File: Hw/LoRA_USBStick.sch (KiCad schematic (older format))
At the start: 16 parts, among them J10 USB_B, J4 SWD, SW1 RST, U1 ATSAMD21E, U2 RFM95W-868S2, U3 AP2112K-3.3

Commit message: add usb c and R
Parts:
- removed J10: USB_B, Connectors:C46394, symbol LoRA_USBStick-rescue:USB_B
- added P1: USB_C_Plug_USB2.0, symbol Connector:USB_C_Plug_USB2.0
- added R1, R2: 5K1, symbol Device:R
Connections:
- wire segments 57 -> 66
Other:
- moved on the sheet: J4
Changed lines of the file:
@@
 EESchema Schematic File Version 4
+LIBS:LoRA_USBStick-cache
 EELAYER 30 0
 EELAYER END
@@
 	1    0    0    -1
 $EndComp
-$Comp
-L LoRA_USBStick-rescue:Conn_01x04 J4
-U 1 1 5B0502EC
-P 6300 4805
-F 0 "J4" H 6300 5005 50  0000 C CNN
-F 1 "SWD" H 6300 4505 50  0000 C CNN
-F 2 "Pin_Headers:Pin_Header_Straight_1x04_Pitch2.54mm" H 6300 4805 50  0001 C CNN
-F 3 "" H 6300 4805 50  0001 C CNN
-	1    6300 4805
-	1    0    0    -1
-$EndComp
-$Comp
-L power:+3.3V #PWR012
-U 1 1 5B050850
-P 5955 4625
-F 0 "#PWR012" H 5955 4475 50  0001 C CNN
-F 1 "+3.3V" H 5955 4765 50  0000 C CNN
-F 2 "" H 5955 4625 50  0001 C CNN
-F 3 "" H 5955 4625 50  0001 C CNN
-	1    5955 4625
-	1    0    0    -1
-$EndComp
-Text Label 5955 4905 2    60   ~ 0
-SWCLK
-Text Label 5955 4805 2    60   ~ 0
-SWDIO
 Text Label 6965 4065 0    60   ~ 0
 SWDIO
@@
 Wire Wire Line
 	4820 1535 4895 1535
-Wire Wire Line
-	6100 4905 5955 4905
-Wire Wire Line
-	5955 4805 6100 4805
-Wire Wire Line
-	6100 4705 5955 4705
-Wire Wire Line
-	5955 4705 5955 4625
-Wire Wire Line
-	5965 5080 5965 5005
-Wire Wire Line
-	5965 5005 6100 5005
 Wire Wire Line
 	7680 725  7680 825
@@
 Wire Notes Line
 	11220 4565 11220 4560
-$Comp
-L power:GND #PWR014
-U 1 1 5B08A6AC
-P 5965 5080
-F 0 "#PWR014" H 5965 4830 50  0001 C CNN
-F 1 "GND" H 5965 4930 50  0000 C CNN
-F 2 "" H 5965 5080 50  0001 C CNN
-F 3 "" H 5965 5080 50  0001 C CNN
-	1    5965 5080
-	1    0    0    -1
-$EndComp
 Text Label 6965 2665 0    60   ~ 0
 RFM_RST
@@
 L power:GND #PWR015
 U 1 1 5B0C9EAC
-P 4805 5395
-F 0 "#PWR015" H 4805 5145 50  0001 C CNN
-F 1 "GND" H 4805 5245 50  0000 C CNN
-F 2 "" H 4805 5395 50  0001 C CNN
-F 3 "" H 4805 5395 50  0001 C CNN
-	1    4805 5395
-	1    0    0    -1
-$EndComp
-Wire Wire Line
-	4805 5395 4805 5350
-Wire Wire Line
-	4905 5290 4905 5350
-Wire Wire Line
-	4905 5350 4805 5350
-Connection ~ 4805 5350
-Text Label 5205 4890 0    60   ~ 0
+P 4780 6236
+F 0 "#PWR015" H 4780 5986 50  0001 C CNN
+F 1 "GND" H 4780 6086 50  0000 C CNN
+F 2 "" H 4780 6236 50  0001 C CNN
+F 3 "" H 4780 6236 50  0001 C CNN
+	1    4780 6236
+	1    0    0    -1
+$EndComp
+Text Label 5528 5292 0    60   ~ 0
 D+
-Text Label 5205 4990 0    60   ~ 0
+Text Label 5528 5092 0    60   ~ 0
 D-
 Text Label 6965 3665 0    60   ~ 0
@@
 Text Label 6965 3565 0    60   ~ 0
 D-
-$Comp
-L power:VBUS #PWR016
-U 1 1 5B0CB923
-P 5285 4630
-F 0 "#PWR016" H 5285 4480 50  0001 C CNN
-F 1 "VBUS" H 5285 4780 50  0000 C CNN
-F 2 "" H 5285 4630 50  0001 C CNN
-F 3 "" H 5285 4630 50  0001 C CNN
-	1    5285 4630
-	1    0    0    -1
-$EndComp
-Wire Wire Line
-	5285 4630 5285 4690
-Wire Wire Line
-	5285 4690 5205 4690
 Text Notes 1165 935  0    60   ~ 0
 USB voltage regulator\n
@@
 NoConn ~ 6965 1865
 NoConn ~ 6965 1165
-$Comp
-L LoRA_USBStick-rescue:USB_B J10
-U 1 1 5B11F4BB
-P 4905 4890
-F 0 "J10" H 4705 5340 50  0000 L CNN
-F 1 "USB_B" H 4705 5240 50  0000 L CNN
-F 2 "Connectors:C46394" H 5055 4840 50  0001 C CNN
-F 3 "" H 5055 4840 50  0001 C CNN
-	1    4905 4890
-	1    0    0    -1
-$EndComp
 Wire Wire Line
 	10750 1950 10750 2050
@@
 	4650 1255 4650 1385
 Wire Wire Line
-	4805 5350 4805 5290
-Wire Wire Line
 	2355 1330 2960 1330
 Wire Wire Line
 	1395 1330 1315 1330
-Wire Notes Line
-	8270 475  8270 6535
 Wire Notes Line
 	2290 2365 2290 6540
@@
 	1565 1430 1565 1330
 Connection ~ 1565 1330
+$Comp
+L Connector:USB_C_Plug_USB2.0 P1
+U 1 1 5F54D8FB
+P 4928 5192
+F 0 "P1" H 5035 6059 50  0000 C CNN
+F 1 "USB_C_Plug_USB2.0" H 5035 5968 50  0000 C CNN
+F 2 "" H 5078 5192 50  0001 C CNN
+F 3 "https://www.usb.org/sites/default/files/documents/usb_type-c.zip" H 5078 5192 50  0001 C CNN
+	1    4928 5192
+	1    0    0    -1
+$EndComp
+$Comp
+L power:VBUS #PWR016
+U 1 1 5B0CB923
+P 5607 4533
+F 0 "#PWR016" H 5607 4383 50  0001 C CNN
+F 1 "VBUS" H 5607 4683 50  0000 C CNN
+F 2 "" H 5607 4533 50  0001 C CNN
+F 3 "" H 5607 4533 50  0001 C CNN
+	1    5607 4533
+	1    0    0    -1
+$EndComp
+Wire Wire Line
+	5607 4533 5607 4592
+Wire Wire Line
+	5607 4592 5528 4592
+Wire Wire Line
+	4628 6092 4628 6161
+Wire Wire Line
+	4628 6161 4780 6161
+Wire Wire Line
+	4928 6092 4928 6161
+Wire Wire Line
+	4780 6236 4780 6161
+Connection ~ 4780 6161
+Wire Wire Line
+	4780 6161 4928 6161
+$Comp
+L Device:R R2
+U 1 1 5F5760B6
+P 5834 4892
+F 0 "R2" V 5912 4893 50  0000 C CNN
+F 1 "5K1" V 5990 4899 50  0000 C CNN
+F 2 "" V 5764 4892 50  0001 C CNN
+F 3 "~" H 5834 4892 50  0001 C CNN
+	1    5834 4892
+	0    1    1    0
+$EndComp
+Wire Wire Line
+	5528 4792 5684 4792
+Wire Wire Line
+	5684 4892 5528 4892
+$Comp
+L power:GND #PWR011
+U 1 1 5F57D4B7
+P 6111 4904
+F 0 "#PWR011" H 6111 4654 50  0001 C CNN
+F 1 "GND" H 6111 4754 50  0000 C CNN
+F 2 "" H 6111 4904 50  0001 C CNN
+F 3 "" H 6111 4904 50  0001 C CNN
+	1    6111 4904
+	1    0    0    -1
+$EndComp
+Wire Wire Line
+	5984 4892 6032 4892
+Wire Wire Line
+	6032 4792 5984 4792
+Wire Wire Line
+	6032 4892 6032 4837
+Wire Wire Line
+	6111 4904 6111 4837
+Wire Wire Line
+	6111 4837 6032 4837
+Connection ~ 6032 4837
+Wire Wire Line
+	6032 4837 6032 4792
+$Comp
+L LoRA_USBStick-rescue:Conn_01x04 J4
+U 1 1 5B0502EC
+P 7145 5321
+F 0 "J4" H 7145 5521 50  0000 C CNN
+F 1 "SWD" H 7145 5021 50  0000 C CNN
+F 2 "Pin_Headers:Pin_Header_Straight_1x04_Pitch2.54mm" H 7145 5321 50  0001 C CNN
+F 3 "" H 7145 5321 50  0001 C CNN
+	1    7145 5321
+	1    0    0    -1
+$EndComp
+$Comp
+L power:+3.3V #PWR012
+U 1 1 5B050850
+P 6800 5141
+F 0 "#PWR012" H 6800 4991 50  0001 C CNN
+F 1 "+3.3V" H 6800 5281 50  0000 C CNN
+F 2 "" H 6800 5141 50  0001 C CNN
+F 3 "" H 6800 5141 50  0001 C CNN
+	1    6800 5141
+	1    0    0    -1
+$EndComp
+Text Label 6800 5421 2    60   ~ 0
+SWCLK
+Text Label 6800 5321 2    60   ~ 0
+SWDIO
+Wire Wire Line
+	6945 5421 6800 5421
+Wire Wire Line
+	6800 5321 6945 5321
+Wire Wire Line
+	6945 5221 6800 5221
+Wire Wire Line
+	6800 5221 6800 5141
+Wire Wire Line
+	6810 5596 6810 5521
+Wire Wire Line
+	6810 5521 6945 5521
+$Comp
+L power:GND #PWR014
+U 1 1 5B08A6AC
+P 6810 5596
+F 0 "#PWR014" H 6810 5346 50  0001 C CNN
+F 1 "GND" H 6810 5446 50  0000 C CNN
+F 2 "" H 6810 5596 50  0001 C CNN
+F 3 "" H 6810 5596 50  0001 C CNN
+	1    6810 5596
+	1    0    0    -1
+$EndComp
+Wire Notes Line
+	8270 475  8270 6535
+$Comp
+L Device:R R1
+U 1 1 5F575919
+P 5834 4792
+F 0 "R1" V 5627 4792 50  0000 C CNN
+F 1 "5K1" V 5718 4792 50  0000 C CNN
+F 2 "" V 5764 4792 50  0001 C CNN
+F 3 "~" H 5834 4792 50  0001 C CNN
+	1    5834 4792
+	0    1    1    0
+$EndComp
 $EndSCHEMATC

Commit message: Change_usb-C
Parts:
- P1: footprint (none) -> Connectors:C393939
- R1, R2: footprint (none) -> Resistor_SMD:R_0603_1608Metric_Pad1.05x0.95mm_HandSolder
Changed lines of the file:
@@
 F 0 "P1" H 5035 6059 50  0000 C CNN
 F 1 "USB_C_Plug_USB2.0" H 5035 5968 50  0000 C CNN
-F 2 "" H 5078 5192 50  0001 C CNN
+F 2 "Connectors:C393939" H 5078 5192 50  0001 C CNN
 F 3 "https://www.usb.org/sites/default/files/documents/usb_type-c.zip" H 5078 5192 50  0001 C CNN
 	1    4928 5192
@@
 F 0 "R2" V 5912 4893 50  0000 C CNN
 F 1 "5K1" V 5990 4899 50  0000 C CNN
-F 2 "" V 5764 4892 50  0001 C CNN
+F 2 "Resistor_SMD:R_0603_1608Metric_Pad1.05x0.95mm_HandSolder" V 5764 4892 50  0001 C CNN
 F 3 "~" H 5834 4892 50  0001 C CNN
 	1    5834 4892
@@
 F 0 "R1" V 5627 4792 50  0000 C CNN
 F 1 "5K1" V 5718 4792 50  0000 C CNN
-F 2 "" V 5764 4792 50  0001 C CNN
+F 2 "Resistor_SMD:R_0603_1608Metric_Pad1.05x0.95mm_HandSolder" V 5764 4792 50  0001 C CNN
 F 3 "~" H 5834 4792 50  0001 C CNN
 	1    5834 4792

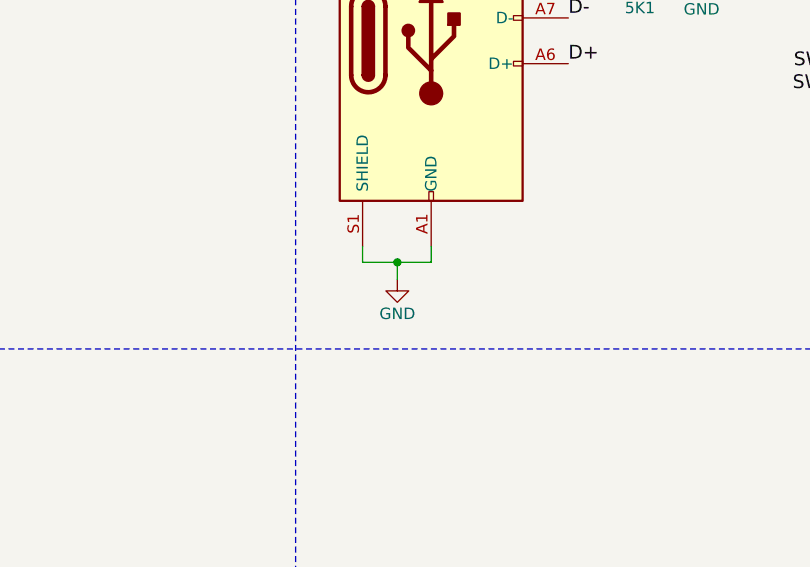
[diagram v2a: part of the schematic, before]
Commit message: Change_in_connector
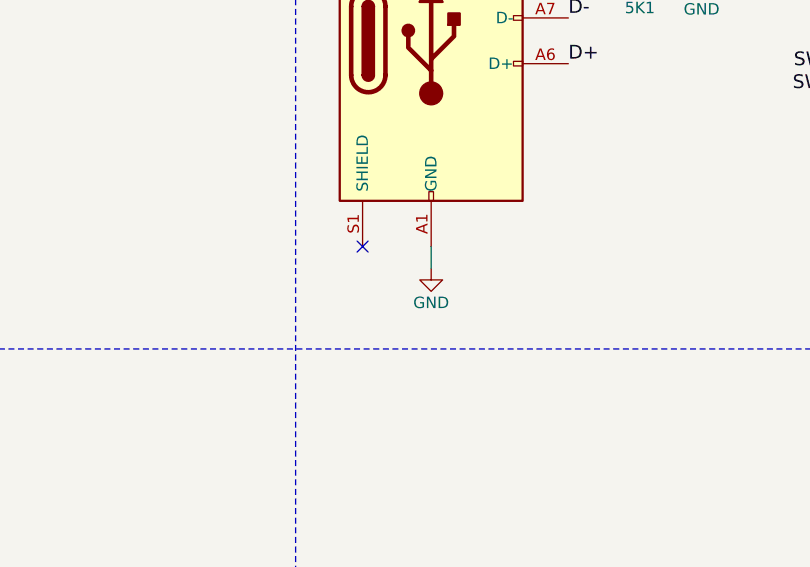
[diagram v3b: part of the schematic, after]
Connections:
- net GND: no longer P1.S1 (SHIELD)
- no-connect marks 14 -> 15
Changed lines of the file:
@@
 EESchema Schematic File Version 4
-LIBS:LoRA_USBStick-cache
 EELAYER 30 0
 EELAYER END
@@
 Text Label 6965 2665 0    60   ~ 0
 RFM_RST
-$Comp
-L power:GND #PWR015
-U 1 1 5B0C9EAC
-P 4780 6236
-F 0 "#PWR015" H 4780 5986 50  0001 C CNN
-F 1 "GND" H 4780 6086 50  0000 C CNN
-F 2 "" H 4780 6236 50  0001 C CNN
-F 3 "" H 4780 6236 50  0001 C CNN
-	1    4780 6236
-	1    0    0    -1
-$EndComp
 Text Label 5528 5292 0    60   ~ 0
 D+
@@
 Wire Wire Line
 	5607 4592 5528 4592
-Wire Wire Line
-	4628 6092 4628 6161
-Wire Wire Line
-	4628 6161 4780 6161
-Wire Wire Line
-	4928 6092 4928 6161
-Wire Wire Line
-	4780 6236 4780 6161
-Connection ~ 4780 6161
-Wire Wire Line
-	4780 6161 4928 6161
 $Comp
 L Device:R R2
@@
 	0    1    1    0
 $EndComp
+$Comp
+L power:GND #PWR015
+U 1 1 5B0C9EAC
+P 4928 6188
+F 0 "#PWR015" H 4928 5938 50  0001 C CNN
+F 1 "GND" H 4928 6038 50  0000 C CNN
+F 2 "" H 4928 6188 50  0001 C CNN
+F 3 "" H 4928 6188 50  0001 C CNN
+	1    4928 6188
+	1    0    0    -1
+$EndComp
+Wire Wire Line
+	4928 6092 4928 6188
+NoConn ~ 4628 6092
 $EndSCHEMATC
